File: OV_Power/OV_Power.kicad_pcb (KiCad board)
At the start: 2 copper layers, 90 x 60 mm, 84 parts, among them CN1 CONN_HEADER_R_A_2POS_2.5MM, J1 Kycon_kpjx-4s, J2 Conn_HDR_2x10_latching, J3 532530670, J4 SpadeLug, J5 SpadeLug, Q1 SSM3K341R, Q2 2N7002BK, U1 LT3796, U2 LT1936, U3 LMC6772AIMX, U4 VNH5019ATR-E, U5 CSD88537ND, U6 LTC4365xTS8, U7 LTC4416, U8 AOSD21307, U9 AOSD21307

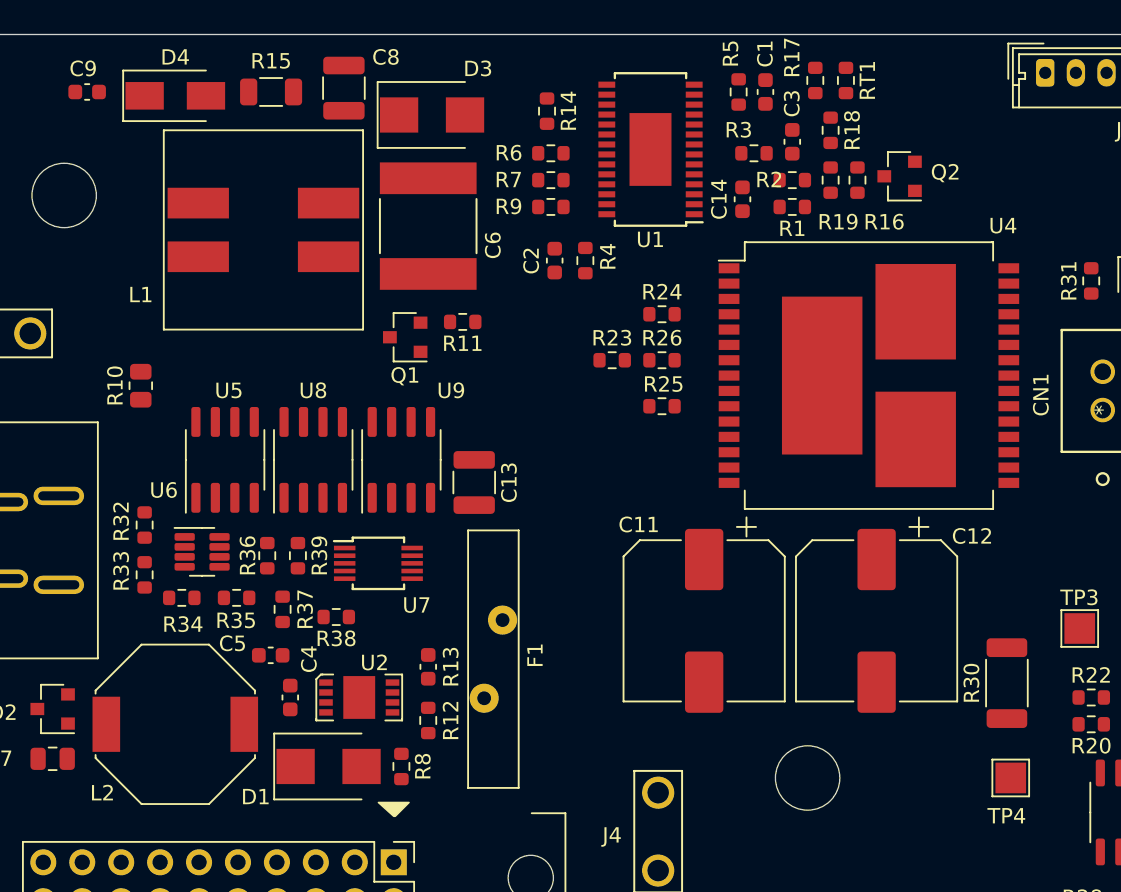
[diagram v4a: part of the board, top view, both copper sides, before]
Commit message: Added two connectors for cooling fans, re-jigged the motor current sensing circuit a bit, still needs a bit of work there.
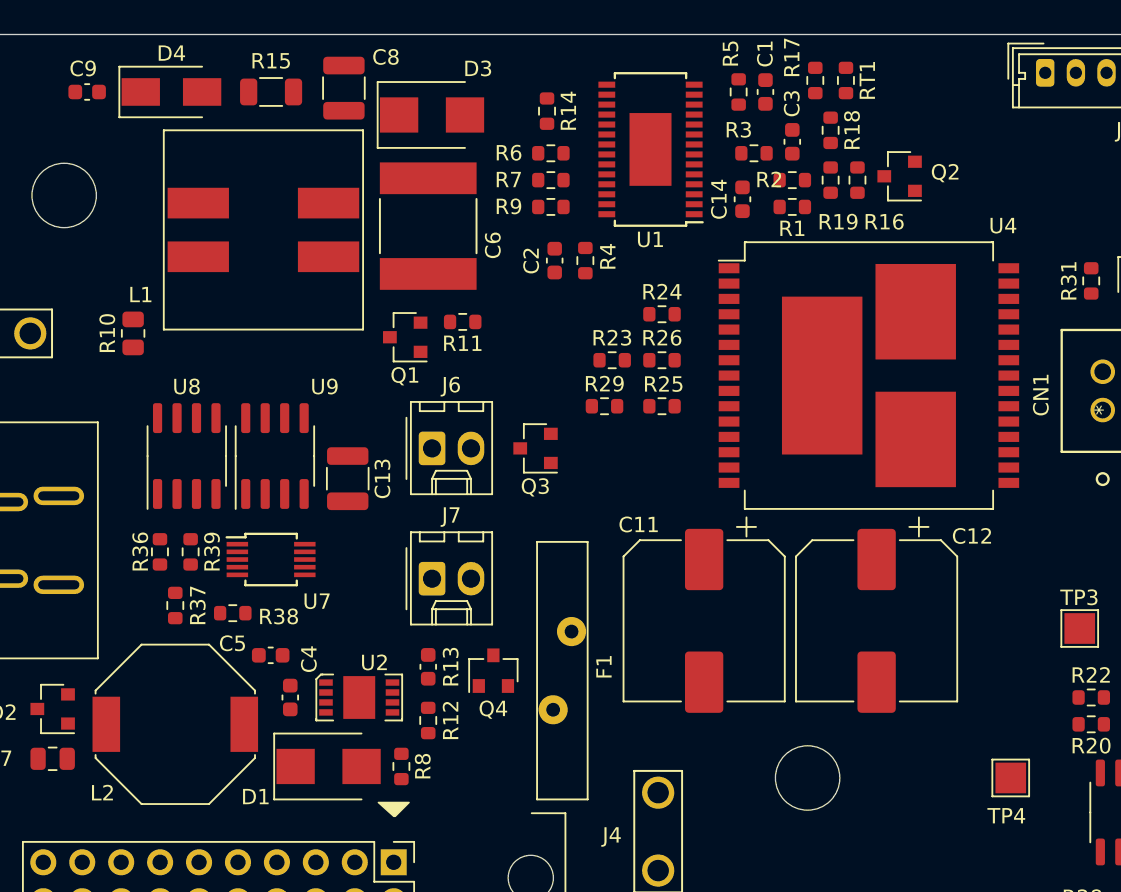
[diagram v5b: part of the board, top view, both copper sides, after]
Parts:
- removed R30: 0.025 Ohm 1W 1%, Resistor_SMD:R_2010_5025Metric
- removed R32: R_0603_4.53M_0.1W_5%, Resistor_SMD:R_0603_1608Metric
- removed R33: R_0603_169K_0.1W_1%, Resistor_SMD:R_0603_1608Metric
- removed R34: R_0603_133K_0.1W_1%, Resistor_SMD:R_0603_1608Metric
- removed R35: R_0603_510K_0.1W_1%, Resistor_SMD:R_0603_1608Metric
- removed U5: CSD88537ND, Package_SO:SOIC-8_3.9x4.9mm_P1.27mm
- removed U6: LTC4365xTS8, Package_TO_SOT_SMD:TSOT-23-8
- added J6: CONN_HEADER_2.54X2_MOLEX_KK_Series, Connector_Molex:Molex_KK-254_AE-6410-02A_1x02_P2.54mm_Vertical, F.Cu at (67.0, 57.0)
- added J7: CONN_HEADER_2.54X2_MOLEX_KK_Series, Connector_Molex:Molex_KK-254_AE-6410-02A_1x02_P2.54mm_Vertical, F.Cu at (67.0, 65.5)
- added Q3: SZNUD3124LT1G, Package_TO_SOT_SMD:SOT-23, F.Cu at (73.8, 57.0)
- added Q4: SZNUD3124LT1G, Package_TO_SOT_SMD:SOT-23, F.Cu at (71.0, 71.5)
- added R29: R_0603_1k5_0.1W_1%, Resistor_SMD:R_0603_1608Metric, F.Cu at (78.2, 54.2)
- D4: value DIODE_GEN_PURP_1KV_1A_SMA -> S1B
- moved C13 8.25 mm to (61.5, 59.0)
- moved U8 8.25 mm to (51.0, 57.5)
- moved U9 8.25 mm to (56.8, 57.5)
- moved R36 7.00 mm to (49.2, 63.8)
- moved R37 7.00 mm to (50.2, 67.2)
- moved R39 7.00 mm to (51.2, 63.8)
- moved U7 7.00 mm to (56.5, 64.2)
- moved R38 6.75 mm to (54.0, 67.8)
- moved F1 4.56 mm to (75.5, 71.5)
- moved R10 3.45 mm to (47.5, 49.5)
- moved D4 0.35 mm to (50.0, 33.8)
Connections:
- D4 pad 1: Net-(D4-Pad1) -> VBATT
- D4 pad 2: VBATT -> Net-(D4-Pad2)
- J2 pad 3: Net-(J2-Pad3) -> /Power Supply/FAN_DRIVE
- R15 pad 2: Net-(D4-Pad1) -> Net-(D4-Pad2)
- R17 pad 1: Net-(D4-Pad1) -> Net-(D4-Pad2)
- R31 pad 1: Net-(R31-Pad1) -> Net-(CN1-Pad2)
- R36 pad 1: VIN_12V -> Net-(J1-Pad1)
- R39 pad 1: VIN_12V -> Net-(J1-Pad1)
- RT1 pad 1: Net-(D4-Pad1) -> Net-(D4-Pad2)
- U1 pad 2: Net-(D4-Pad1) -> Net-(D4-Pad2)
- U4 pad 18: Net-(R20-Pad2) -> GND
- U4 pad 19: Net-(R20-Pad2) -> GND
- U4 pad 20: Net-(R20-Pad2) -> GND
- U4 pad 26: Net-(R20-Pad2) -> GND
- U4 pad 27: Net-(R20-Pad2) -> GND
- U4 pad 28: Net-(R20-Pad2) -> GND
- U4 pad 6: Net-(U4-Pad6) -> GND
- U4 pad 8: Net-(U4-Pad8) -> Net-(R20-Pad2)
- U7 pad 9: VIN_12V -> Net-(J1-Pad1)
- U8 pad 1: VIN_12V -> Net-(J1-Pad1)

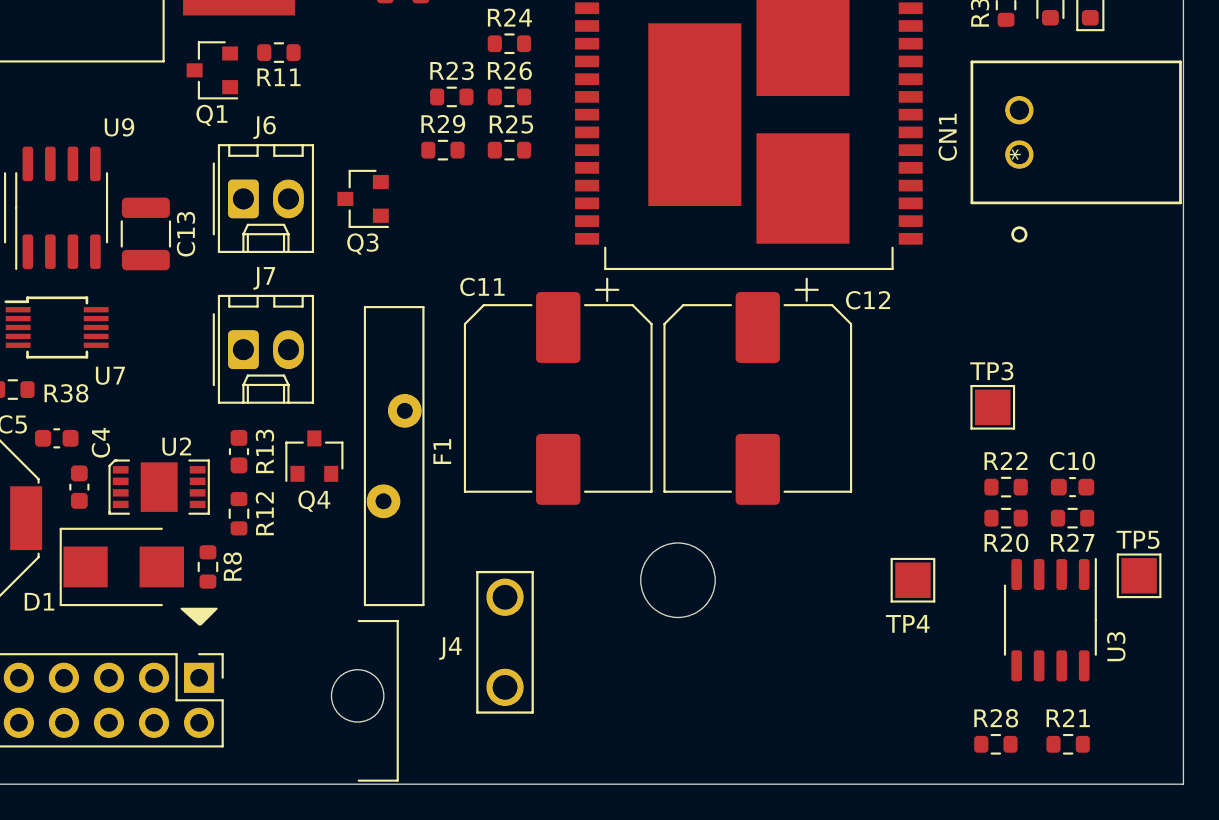
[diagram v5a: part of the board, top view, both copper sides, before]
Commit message: Finished schemo and placement of power supply board, then resolved interconnects with the main board.
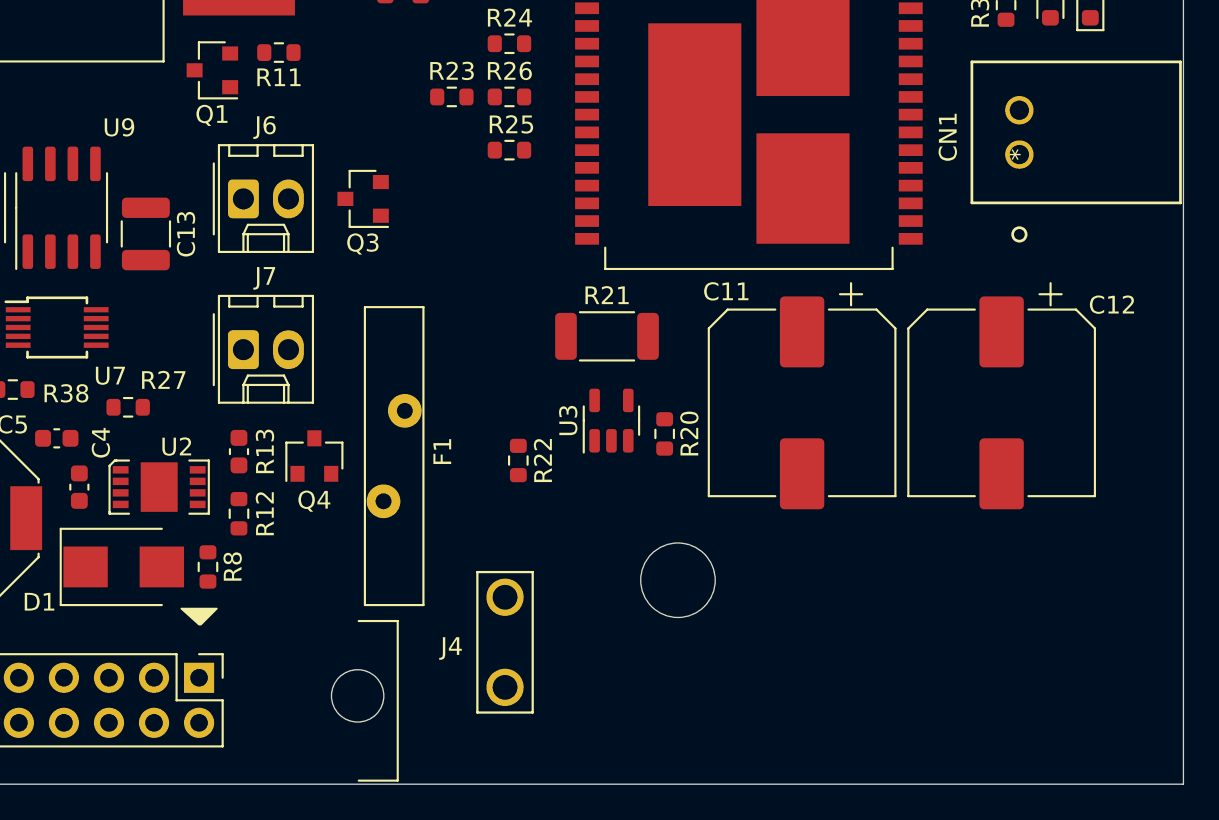
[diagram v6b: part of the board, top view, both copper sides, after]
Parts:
- removed C10: 470pF_0603_Ceramic_Capacitor,_5%,_100V,_C0G, Capacitor_SMD:C_0603_1608Metric
- removed R28: 10k_0603_Chip_Resistor,_1%,_0.1W, Resistor_SMD:R_0603_1608Metric
- removed R29: R_0603_1k5_0.1W_1%, Resistor_SMD:R_0603_1608Metric
- removed TP3, TP4, TP5: Test_Point_PTH, TestPoint:TestPoint_Pad_2.0x2.0mm
- R20: value 10k_0603_Chip_Resistor,_1%,_0.1W -> R_0603_100_0.1W_0.1%
- R21: value 10k_0603_Chip_Resistor,_1%,_0.1W -> 0.025 Ohm; footprint Resistor_SMD:R_0603_1608Metric -> Resistor_SMD:R_2010_5025Metric
- R22: value 10k_0603_Chip_Resistor,_1%,_0.1W -> R_0603_1k2_0.1W_0.1%
- R27: value 215k_0603_Chip_Resistor,_1%,_0.1W -> 1K_0603_Chip_Resistor,_1%,_0.1W
- U3: value LMC6772AIMX -> LT6106; footprint Package_SO:SO-8_3.9x4.9mm_P1.27mm -> Package_TO_SOT_SMD:TSOT-23-5
- moved R27 53.6 mm to (60.5, 68.8)
- moved R21 34.7 mm to (87.5, 64.8)
- moved R22 27.5 mm to (82.5, 71.8), turned to 270 degrees
- moved U3 27.2 mm to (87.8, 69.5), turned to 90 degrees
- moved R20 19.8 mm to (90.8, 70.2), turned to 270 degrees
- moved C11 13.8 mm to (98.5, 68.5)
- moved C12 13.8 mm to (109.8, 68.5)
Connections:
- C11 pad 1: V_MAIN -> Net-(C11-Pad1)
- C12 pad 1: V_MAIN -> Net-(C11-Pad1)
- J2 pad 11: VIN_12V -> /Power Supply/POWER_STATUS
- J2 pad 13: MOTOR-CURRENT -> MOTOR_CURRENT
- J2 pad 17: CHG_CURRENT -> V_MAIN
- J2 pad 18: V7.5V -> CHG_CURRENT
- J2 pad 2: V_MAIN -> V7.5V
- R20 pad 1: Net-(R20-Pad1) -> V_MAIN
- R21 pad 1: Net-(R21-Pad1) -> V_MAIN
- R21 pad 2: +3V3 -> Net-(C11-Pad1)
- R22 pad 1: Net-(C10-Pad1) -> MOTOR_CURRENT
- R27 pad 1: MOTOR-CURRENT -> /Power Supply/POWER_STATUS
- R27 pad 2: Net-(C10-Pad1) -> Net-(R27-Pad2)
- R38 pad 1: Net-(R38-Pad1) -> Net-(R27-Pad2)
- R4 pad 1: Net-(R4-Pad1) -> Net-(C2-Pad1)
- U3 pad 1: MOTOR-CURRENT -> MOTOR_CURRENT
- U3 pad 2: Net-(C10-Pad1) -> GND
- U3 pad 3: Net-(R20-Pad1) -> Net-(R20-Pad2)
- U3 pad 4: GND -> Net-(C11-Pad1)
- U3 pad 5: Net-(R28-Pad2) -> V_MAIN
- U4 pad 13: V_MAIN -> Net-(C11-Pad1)
- U4 pad 23: V_MAIN -> Net-(C11-Pad1)
- U4 pad 3: V_MAIN -> Net-(C11-Pad1)
- U4 pad 31: V_MAIN -> Net-(C11-Pad1)
- U4 pad 6: GND -> Net-(U4-Pad6)
- U4 pad 8: Net-(R20-Pad2) -> Net-(U4-Pad8)
- U7 pad 5: Net-(R38-Pad1) -> Net-(R27-Pad2)

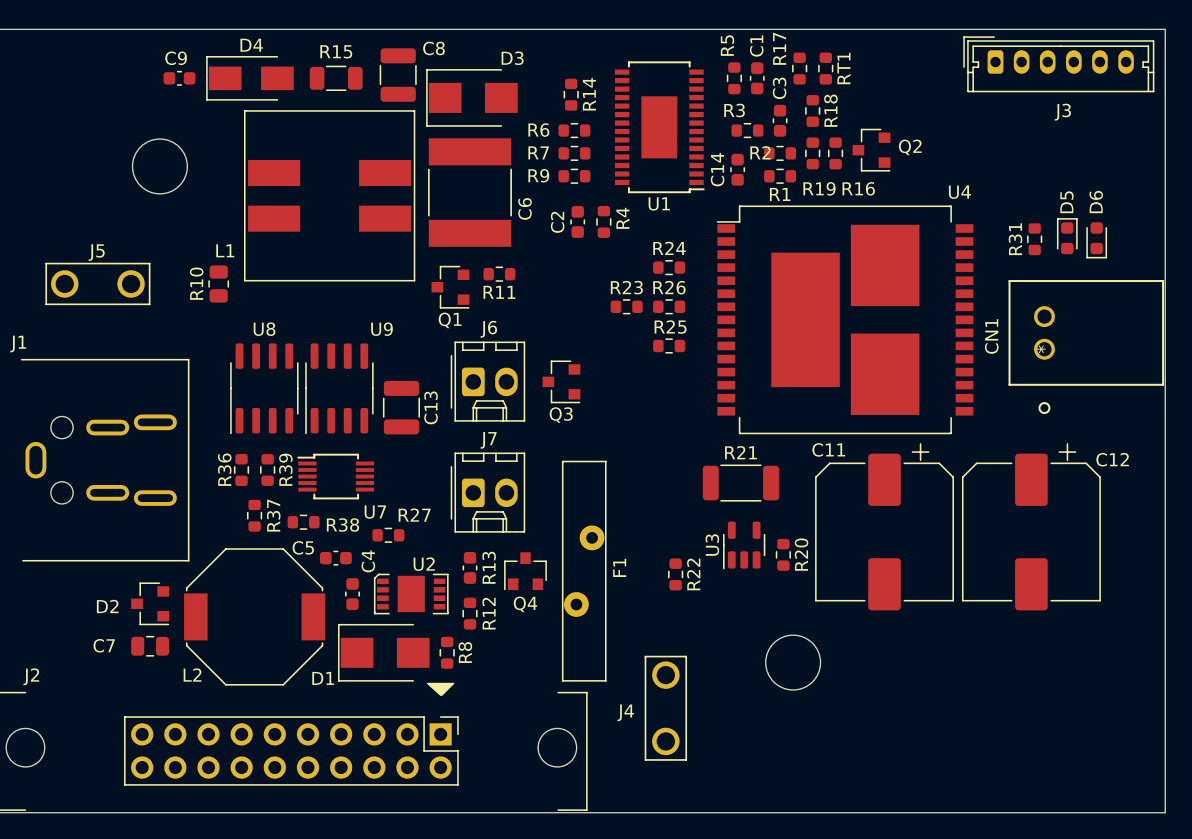
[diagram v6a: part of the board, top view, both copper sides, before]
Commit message: First cut at complete routing for the power board.  Still need DRC checking and final fettling of the BOM and silkscreens before going to press.
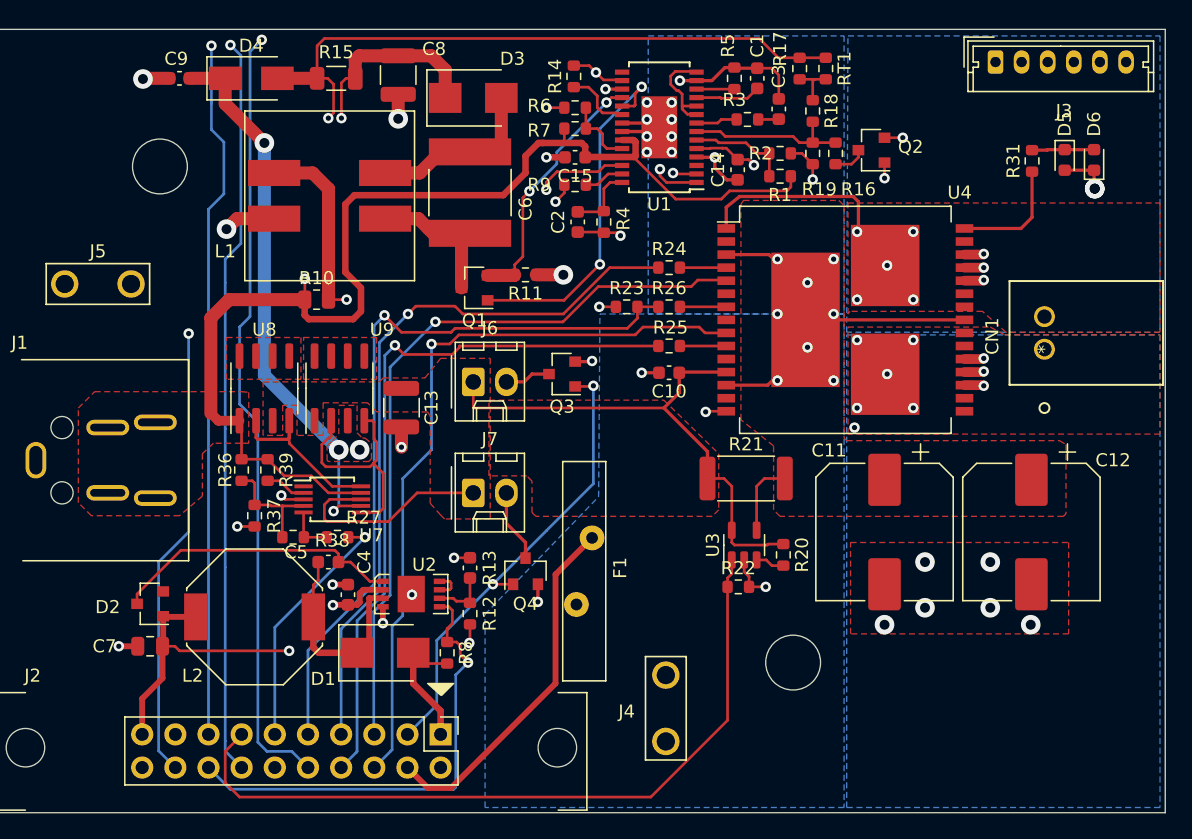
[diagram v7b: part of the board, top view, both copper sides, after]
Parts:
- added C10: 100nF_0603_Ceramic_Capacitor,_10%,_X7R,_25V, Capacitor_SMD:C_0603_1608Metric, F.Cu at (82.0, 56.3)
- added C15: 100nF_0603_Ceramic_Capacitor,_10%,_X7R,_25V, Capacitor_SMD:C_0603_1608Metric, F.Cu at (74.8, 39.8)
- R21: value 0.025 Ohm -> R_2512_15m_cursense; footprint Resistor_SMD:R_2010_5025Metric -> Resistor_SMD:R_2512_6332Metric
- R22: value R_0603_1k2_0.1W_0.1% -> R_0603_2k74_0.1W_0.1%
- moved R10 7.60 mm to (55.0, 50.7), turned to 0 degrees
- moved D5 6.00 mm to (112.3, 40.0)
- moved D6 6.00 mm to (114.5, 40.0)
- moved R31 6.00 mm to (109.8, 40.1)
- moved R22 4.89 mm to (87.3, 72.7), turned to 0 degrees
- moved R27 3.90 mm to (56.6, 68.9)
- moved R11 2.00 mm to (71.0, 48.8)
- moved R6 1.90 mm to (74.8, 37.6)
- moved Q1 1.85 mm to (67.1, 49.8)
- moved U7 1.78 mm to (56.2, 66.0)
- moved R7 1.75 mm to (74.8, 36.0)
- moved R14 1.41 mm to (74.7, 33.6), turned to 90 degrees
- moved R38 1.40 mm to (53.2, 68.9)
- moved C3 0.91 mm to (90.4, 36.1)
- moved R3 0.85 mm to (88.0, 36.9)
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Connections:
- J1 pad 1: Net-(J1-Pad1) -> VIN_12V
- J1 pad 4: Net-(J1-Pad1) -> VIN_12V
- J4 pad 2: (no net) -> Net-(F1-Pad1)
- J5 pad 2: (no net) -> GND
- R36 pad 1: Net-(J1-Pad1) -> VIN_12V
- R39 pad 1: Net-(J1-Pad1) -> VIN_12V
- U7 pad 9: Net-(J1-Pad1) -> VIN_12V
- U8 pad 1: Net-(J1-Pad1) -> VIN_12V
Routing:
- net Net-(J2-Pad15): track 0.00 -> 121.8 mm, vias 0 -> 1
- net Net-(J2-Pad14): track 0.00 -> 120.9 mm, vias 0 -> 1
- net Net-(J2-Pad10): track 0.00 -> 117.0 mm, vias 0 -> 1
- net VIN_12V: track 0.00 -> 116.5 mm, vias 0 -> 2
- net V_MAIN: track 0.00 -> 96.0 mm, vias 0 -> 1
- net CHG_CURRENT: track 0.00 -> 88.3 mm, vias 0 -> 2
- net Net-(D4-Pad2): track 0.00 -> 79.9 mm, vias 0 -> 2
- net GND: track 0.00 -> 78.6 mm, vias 0 -> 45
- net VBATT: track 0.00 -> 69.5 mm, vias 0 -> 4
- net V7.5V: track 0.00 -> 68.0 mm, vias 0 -> 2
- net MOTOR_CURRENT: track 0.00 -> 58.0 mm
- net nMOTOR-FAULT-B: track 0.00 -> 57.6 mm, vias 0 -> 1
- net PWM: track 0.00 -> 57.5 mm, vias 0 -> 1
- net nMOTOR-FAULT-A: track 0.00 -> 57.2 mm, vias 0 -> 1
- net MOTOR-IN-A: track 0.00 -> 55.5 mm, vias 0 -> 1
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- added copper zone on F.Cu, net GND
- added copper zone on In1.Cu, net GND
- added copper zone on B.Cu, net Net-(C11-Pad1)
- added copper zone on F.Cu, net Net-(C11-Pad1)
- added copper zone on B.Cu, net Net-(CN1-Pad1)
- added copper zone on F.Cu, net Net-(CN1-Pad1)
- added copper zone on B.Cu, net Net-(CN1-Pad2)
- added copper zone on F.Cu, net Net-(CN1-Pad2)
- added copper zone on In2.Cu, net Net-(F1-Pad1)
- added copper zone on F.Cu, net Net-(U8-Pad5)
- added copper zone on F.Cu, net Net-(U9-Pad5)
- added copper zone on F.Cu, net VBATT
- added copper zone on In2.Cu, net VBATT
- added copper zone on F.Cu, net VIN_12V
- added copper zone on F.Cu, net V_MAIN
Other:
- copper layers 2 -> 4
- rule trace_min: 0.2 -> 0.153
